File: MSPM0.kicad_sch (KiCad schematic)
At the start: 11 parts, among them U1 MSPM0G3507SPTR, X1 8MHz

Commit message: Finished schematic!!
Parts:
- added C10, C9: 10u, Capacitor_SMD:C_0805_2012Metric, symbol Device:C
- added C11, C12, C13, C14, C7, C8: 470n, Capacitor_SMD:C_0201_0603Metric, symbol Device:C
- added D1: USBLC6-2SC6, Package_TO_SOT_SMD:SOT-23-6, symbol Power_Protection:USBLC6-2SC6
- added FID1, FID2, FID3: Fiducial, Fiducial:Fiducial_1mm_Mask2mm, symbol Mechanical:Fiducial
- added J1: USB4105-GF-A, Connector_USB:USB_C_Receptacle_GCT_USB4105-xx-A_16P_TopMnt_Horizontal, symbol Connector:USB_C_Receptacle_USB2.0_16P
- added J2: TC2030, Connector:Tag-Connect_TC2030-IDC-FP_2x03_P1.27mm_Vertical, symbol Connector:Conn_ARM_SWD_TagConnect_TC2030
- added MH1, MH2, MH3, MH4: M3, MountingHole:MountingHole_3.2mm_M3_Pad_Via, symbol Mechanical:MountingHole_Pad
- added R4: 0R, Resistor_SMD:R_0201_0603Metric, symbol Device:R
- added R5, R6, R7, R8: 5k1, Resistor_SMD:R_0201_0603Metric, symbol Device:R
- added U2: SPX3819M5-L-3-3, Package_TO_SOT_SMD:SOT-23-5, symbol Regulator_Linear:SPX3819M5-L-3-3
- added U3: CH340E, Package_SO:MSOP-10_3x3mm_P0.5mm, symbol Interface_USB:CH340E
- added U4: LIS2DH, Package_LGA:LGA-14_2x2mm_P0.35mm_LayoutBorder3x4y, symbol Sensor_Motion:LIS2DH
- X1: footprint Crystal:Crystal_SMD_Abracon_ABM8AIG-4Pin_3.2x2.5mm -> Crystal:Crystal_SMD_3225-4Pin_3.2x2.5mm
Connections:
- net +3V3: now also C10.1, C12.1, C13.1, C14.1, J2.1 (VCC), R7.1, R8.1, U2.5 (OUT), U3.10 (V3), U3.7 (VCC), U4.4 (~{CS}), U4.7 (Vdd_IO), U4.8 (Vdd)
- net GND: now also C4.2, C10.2, C11.2, C12.2, C13.2, C14.2, C7.2, C8.2, C9.2, D1.2 (GND), J1.A1 (GND), J1.A12 (GND), J1.B1 (GND), J1.B12 (GND), J1.SH (SHIELD), J2.5 (GND), MH1.1, MH2.1, MH3.1, MH4.1, R5.2, R6.2, U2.2 (GND), U3.3 (GND), U4.10 (GND), U4.11 (GND), U4.12 (GND), U4.13 (GND), U4.14 (GND), U4.3 (SDO), U4.9 (GND)
- net NRST: now also J2.3 (~{RESET})
- net VREF+: now also C3.2, U1.43 (PA23/VREF+)
- net UART0_TX: now reaches U1.1 (PA0)
- net UART0_TX: now also U3.9 (RXD)
- net I2C1_SCL: now reaches U1.14 (PB2)
- net I2C1_SCL: now also R7.2, U4.1 (SCL/SPC)
- net I2C1_SDA: now reaches U1.15 (PB3)
- net I2C1_SDA: now also R8.2, U4.2 (SDA/SDI)
- net UART0_RTS: now reaches U1.16 (PA8)
- net UART0_RTS: now also U3.5 (~{CTS})
- net UART0_CTS: now reaches U1.17 (PA9)
- net UART0_CTS: now also U3.4 (~{RTS})
- net UART0_RX: now reaches U1.2 (PA1)
- net UART0_RX: now also U3.8 (TXD)
- net INT1: now reaches U1.24 (PB14)
- net INT1: now also U4.6 (INT1)
- net INT2: now reaches U1.25 (PB15)
- net INT2: now also U4.5 (INT2)
- net at U1.34 (PA19/SWDIO): now also J2.2 (SWDIO)
- net at U1.35 (PA20/SWCLK): now also J2.4 (SWCLK)
- new net: C11.1, U2.4 (BP)
- new net +VBUS: C7.1, D1.5 (VBUS), J1.A4 (VBUS), J1.A9 (VBUS), J1.B4 (VBUS), J1.B9 (VBUS), R4.1
- new net +VBUSF: C8.1, C9.1, R4.2, U2.1 (IN), U2.3 (EN)
- new net USBC_D+: D1.3 (I/O2), J1.A6 (D+), J1.B6 (D+)
- new net USBC_D-: D1.1 (I/O1), J1.A7 (D-), J1.B7 (D-)
- new net USB_CC1: J1.A5 (CC1), R6.1
- new net USB_CC2: J1.B5 (CC2), R5.1
- new net USB_D+: D1.4 (I/O2), U3.1 (UD+)
- new net USB_D-: D1.6 (I/O1), U3.2 (UD-)
- no-connect marks 0 -> 33
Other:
- note added: "+3V3 LDO Regulator"
- note added: "Accelerometer"
- note added: "Assumed stray capacitance of 3-5pF Connected D- and D+ together because two ways of USB-C"
- note added: "MSPM0 MCU"
- note added: "SWD Header"
- note added: "USB-C Connector"
- note added: "USB-UART Converter"
- note removed: "Assumed stray capacitance of 3-5pF"
- title: Microcontroller_Demo -> MSPM0_Schematic
- moved on the sheet: C1, C2, C3, C4, C5, C6, R1, R2, R3, U1, X1

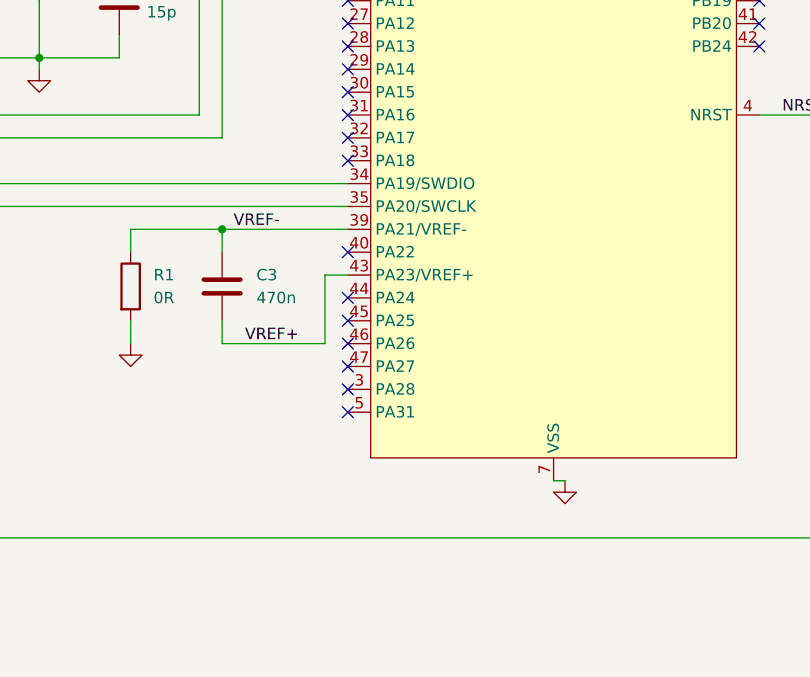
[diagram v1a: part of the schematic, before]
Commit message: Started PCB, fixed schematic footprints Added colors
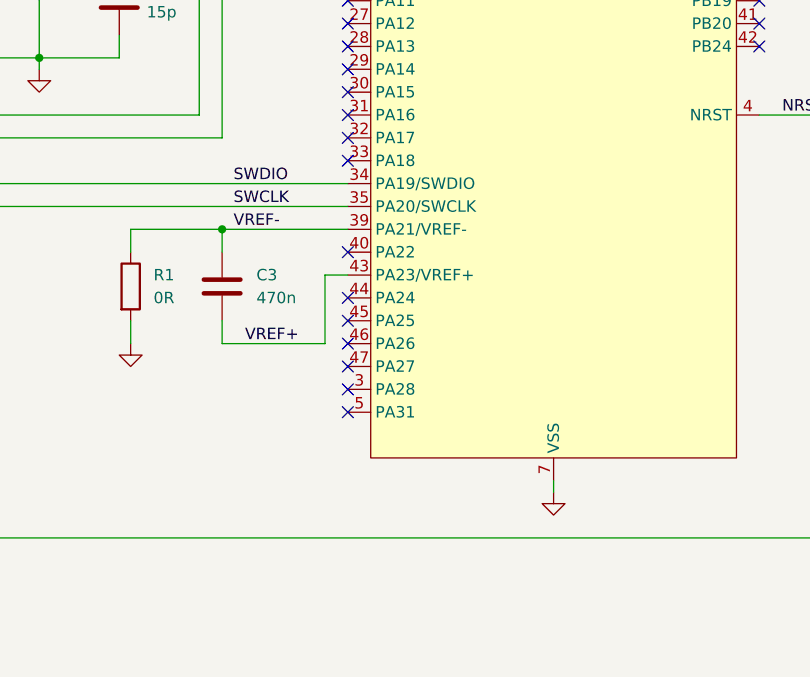
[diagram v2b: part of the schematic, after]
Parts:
- C5, C6: footprint Capacitor_SMD:C_0805_2012Metric -> Capacitor_SMD:C_0201_0603Metric
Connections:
- net SWDIO: now reaches J2.2 (SWDIO), U1.34 (PA19/SWDIO)
- net SWCLK: now reaches J2.4 (SWCLK), U1.35 (PA20/SWCLK)
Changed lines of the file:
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@@
 	(wire
 		(pts
-			(xy 213.36 144.78) (xy 214.63 144.78)
+			(xy 213.36 144.78) (xy 213.36 146.05)
 		)
 		(stroke
@@
 		)
 	)
+	(label "SWCLK"
+		(at 177.8 114.3 0)
+		(effects
+			(font
+				(size 1.27 1.27)
+			)
+			(justify left bottom)
+		)
+	)
 	(label "UART0_TX"
 		(at 180.34 63.5 0)
@@
 		)
 	)
+	(label "SWDIO"
+		(at 177.8 111.76 0)
+		(effects
+			(font
+				(size 1.27 1.27)
+			)
+			(justify left bottom)
+		)
+	)
 	(label "ROSC"
 		(at 184.15 68.58 0)
@@
 	(symbol
 		(lib_id "power:GND")
-		(at 214.63 144.78 0)
+		(at 213.36 146.05 0)
 		(unit 1)
 		(body_style 1)
@@
 		(fields_autoplaced yes)
 		(property "Reference" "#PWR01"
-			(at 214.63 151.13 0)
+			(at 213.36 152.4 0)
 			(hide yes)
 			(show_name no)
@@
 		)
 		(property "Value" "GND"
-			(at 214.63 149.86 0)
+			(at 213.36 151.13 0)
 			(hide yes)
 			(show_name no)
@@
 		)
 		(property "Footprint" ""
-			(at 214.63 144.78 0)
+			(at 213.36 146.05 0)
 			(hide yes)
 			(show_name no)
@@
 		)
 		(property "Datasheet" ""
-			(at 214.63 144.78 0)
+			(at 213.36 146.05 0)
 			(hide yes)
 			(show_name no)
@@
 		)
 		(property "Description" "Power symbol creates a global label with name \"GND\" , ground"
-			(at 214.63 144.78 0)
+			(at 213.36 146.05 0)
 			(hide yes)
 			(show_name no)
@@
 			)
 		)
-		(property "Footprint" "Capacitor_SMD:C_0805_2012Metric"
+		(property "Footprint" "Capacitor_SMD:C_0201_0603Metric"
 			(at 148.2852 95.25 0)
 			(hide yes)
@@
 			)
 		)
-		(property "Footprint" "Capacitor_SMD:C_0805_2012Metric"
+		(property "Footprint" "Capacitor_SMD:C_0201_0603Metric"
 			(at 166.0652 95.25 0)
 			(hide yes)

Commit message: Positioned components, made schematic adjustment accordingly Created ground layer
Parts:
- C1, C10, C9: KiLib_Generator (none) -> SMD_2terminal_chip_molded
- C11, C12, C13, C14, C2, C3, C4, C5, C6, C7, C8: footprint Capacitor_SMD:C_0201_0603Metric -> Capacitor_SMD:C_0603_1608Metric; KiLib_Generator (none) -> SMD_2terminal_chip_molded
- D1, U1, U2, U3: KiLib_Generator (none) -> package/gullwing
- FID1, FID2, FID3: KiLib_Generator (none) -> fiducial
- MH1, MH2, MH3, MH4: KiLib_Generator (none) -> mounting_hardware/mounting_hole
- R1, R2, R3, R4, R5, R6, R7, R8: footprint Resistor_SMD:R_0201_0603Metric -> Capacitor_SMD:C_0603_1608Metric; KiLib_Generator (none) -> SMD_2terminal_chip_molded
- U4: KiLib_Generator (none) -> package/no_lead
- X1: KiLib_Generator (none) -> crystal_resonator_oscillator; private KLC_S4.1 -> (none)
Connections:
- net INT1: now also U1.22 (PB8); no longer U1.24 (PB14)
- net INT2: now also U1.23 (PB9); no longer U1.25 (PB15)
- net USBC_D+: now also D1.1 (I/O1); no longer D1.3 (I/O2)
- net USBC_D-: now also D1.3 (I/O2); no longer D1.1 (I/O1)
- net USB_D+: now also D1.6 (I/O1); no longer D1.4 (I/O2)
- net USB_D-: now also D1.4 (I/O2); no longer D1.6 (I/O1)
- net I2C0_SDA: now reaches U1.18 (PA10)
- net I2C0_SDA: now also R8.2, U4.2 (SDA/SDI)
- net I2C0_SCL: now reaches U1.19 (PA11)
- net I2C0_SCL: now also R7.2, U4.1 (SCL/SPC)
- removed net I2C1_SCL: R7.2, U1.14 (PB2), U4.1 (SCL/SPC)
- removed net I2C1_SDA: R8.2, U1.15 (PB3), U4.2 (SDA/SDI)
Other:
- note added: "To MCU"
- note added: "To/From MCU"
- moved on the sheet: C14, R7, R8, U4

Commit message: Completed mk. I
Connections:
- net USBC_D+: now also D1.3 (I/O2); no longer D1.1 (I/O1)
- net USBC_D-: now also D1.1 (I/O1); no longer D1.3 (I/O2)
- net USB_D+: now also D1.4 (I/O2); no longer D1.6 (I/O1)
- net USB_D-: now also D1.6 (I/O1); no longer D1.4 (I/O2)
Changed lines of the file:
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@@
+	)
+	(junction
+		(at 49.53 54.61)
+		(diameter 0)
+		(color 0 0 0 0)
 	)
 	(junction
@@
 	)
 	(junction
+		(at 49.53 52.07)
+		(diameter 0)
+		(color 0 0 0 0)
+	)
+	(junction
 		(at 43.18 187.96)
 		(diameter 0)
@@
 	)
 	(junction
-		(at 49.53 54.61)
-		(diameter 0)
-		(color 0 0 0 0)
-	)
-	(junction
-		(at 49.53 49.53)
-		(diameter 0)
-		(color 0 0 0 0)
-	)
-	(junction
 		(at 90.17 57.15)
 		(diameter 0)
@@
 	(wire
 		(pts
-			(xy 81.28 73.66) (xy 81.28 54.61)
-		)
-		(stroke
-			(width 0)
-			(type default)
-		)
-	)
-	(wire
-		(pts
 			(xy 71.12 127) (xy 71.12 128.27)
 		)
@@
 	(wire
 		(pts
-			(xy 83.82 52.07) (xy 76.2 52.07)
-		)
-		(stroke
-			(width 0)
-			(type default)
-		)
-	)
-	(wire
-		(pts
 			(xy 172.72 83.82) (xy 190.5 83.82)
 		)
@@
 	(wire
 		(pts
+			(xy 49.53 54.61) (xy 66.04 54.61)
+		)
+		(stroke
+			(width 0)
+			(type default)
+		)
+	)
+	(wire
+		(pts
+			(xy 83.82 54.61) (xy 76.2 54.61)
+		)
+		(stroke
+			(width 0)
+			(type default)
+		)
+	)
+	(wire
+		(pts
 			(xy 46.99 49.53) (xy 49.53 49.53)
 		)
@@
 	(wire
 		(pts
-			(xy 59.69 52.07) (xy 59.69 54.61)
-		)
-		(stroke
-			(width 0)
-			(type default)
-		)
-	)
-	(wire
-		(pts
 			(xy 109.22 26.67) (xy 110.49 26.67)
 		)
@@
 	(wire
 		(pts
-			(xy 66.04 54.61) (xy 63.5 54.61)
-		)
-		(stroke
-			(width 0)
-			(type default)
-		)
-	)
-	(wire
-		(pts
 			(xy 176.53 116.84) (xy 176.53 119.38)
 		)
@@
 	(wire
 		(pts
+			(xy 81.28 52.07) (xy 76.2 52.07)
+		)
+		(stroke
+			(width 0)
+			(type default)
+		)
+	)
+	(wire
+		(pts
 			(xy 247.65 92.71) (xy 247.65 93.98)
 		)
@@
 	(wire
 		(pts
-			(xy 66.04 52.07) (xy 59.69 52.07)
-		)
-		(stroke
-			(width 0)
-			(type default)
-		)
-	)
-	(wire
-		(pts
 			(xy 63.5 26.67) (xy 68.58 26.67)
 		)
@@
 	(wire
 		(pts
-			(xy 59.69 54.61) (xy 49.53 54.61)
-		)
-		(stroke
-			(width 0)
-			(type default)
-		)
-	)
-	(wire
-		(pts
 			(xy 60.96 140.97) (xy 59.69 140.97)
 		)
@@
 	(wire
 		(pts
-			(xy 63.5 49.53) (xy 49.53 49.53)
-		)
-		(stroke
-			(width 0)
-			(type default)
-		)
-	)
-	(wire
-		(pts
 			(xy 60.96 127) (xy 60.96 128.27)
 		)
@@
 	(wire
 		(pts
+			(xy 81.28 73.66) (xy 81.28 52.07)
+		)
+		(stroke
+			(width 0)
+			(type default)
+		)
+	)
+	(wire
+		(pts
 			(xy 147.32 86.36) (xy 147.32 76.2)
 		)
@@
 	(wire
 		(pts
+			(xy 49.53 52.07) (xy 66.04 52.07)
+		)
+		(stroke
+			(width 0)
+			(type default)
+		)
+	)
+	(wire
+		(pts
 			(xy 227.33 49.53) (xy 227.33 50.8)
 		)
@@
 	(wire
 		(pts
-			(xy 81.28 54.61) (xy 76.2 54.61)
-		)
-		(stroke
-			(width 0)
-			(type default)
-		)
-	)
-	(wire
-		(pts
 			(xy 41.91 130.81) (xy 41.91 133.35)
 		)
@@
 	(wire
 		(pts
-			(xy 63.5 54.61) (xy 63.5 49.53)
-		)
-		(stroke
-			(width 0)
-			(type default)
-		)
-	)
-	(wire
-		(pts
 			(xy 236.22 76.2) (xy 243.84 76.2)
 		)
@@
 	(wire
 		(pts
-			(xy 83.82 71.12) (xy 83.82 52.07)
-		)
-		(stroke
-			(width 0)
-			(type default)
-		)
-	)
-	(wire
-		(pts
 			(xy 135.89 121.92) (xy 135.89 151.13)
 		)
@@
 		(pts
 			(xy 58.42 44.45) (xy 58.42 26.67)
+		)
+		(stroke
+			(width 0)
+			(type default)
+		)
+	)
+	(wire
+		(pts
+			(xy 83.82 71.12) (xy 83.82 54.61)
 		)
 		(stroke
@@
 		)
 	)
+	(label "USBC_D-"
+		(at 50.8 52.07 0)
+		(effects
+			(font
+				(size 1.27 1.27)
+			)
+			(justify left bottom)
+		)
+	)
 	(label "HFXIN"
 		(at 184.15 76.2 0)
@@
 	)
 	(label "USBC_D+"
-		(at 49.53 54.61 0)
+		(at 50.8 54.61 0)
 		(effects
 			(font
-				(size 1.27 1.27)
-			)
-			(justify left bottom)
-		)
-	)
-	(label "USBC_D-"
-		(at 49.53 52.07 0)
-		(effects
-			(font
